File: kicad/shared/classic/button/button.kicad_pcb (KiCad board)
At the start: 2 copper layers, 22 x 45 mm, 6 parts, among them J2 Screw_Terminal_01x03, Q1 BC547

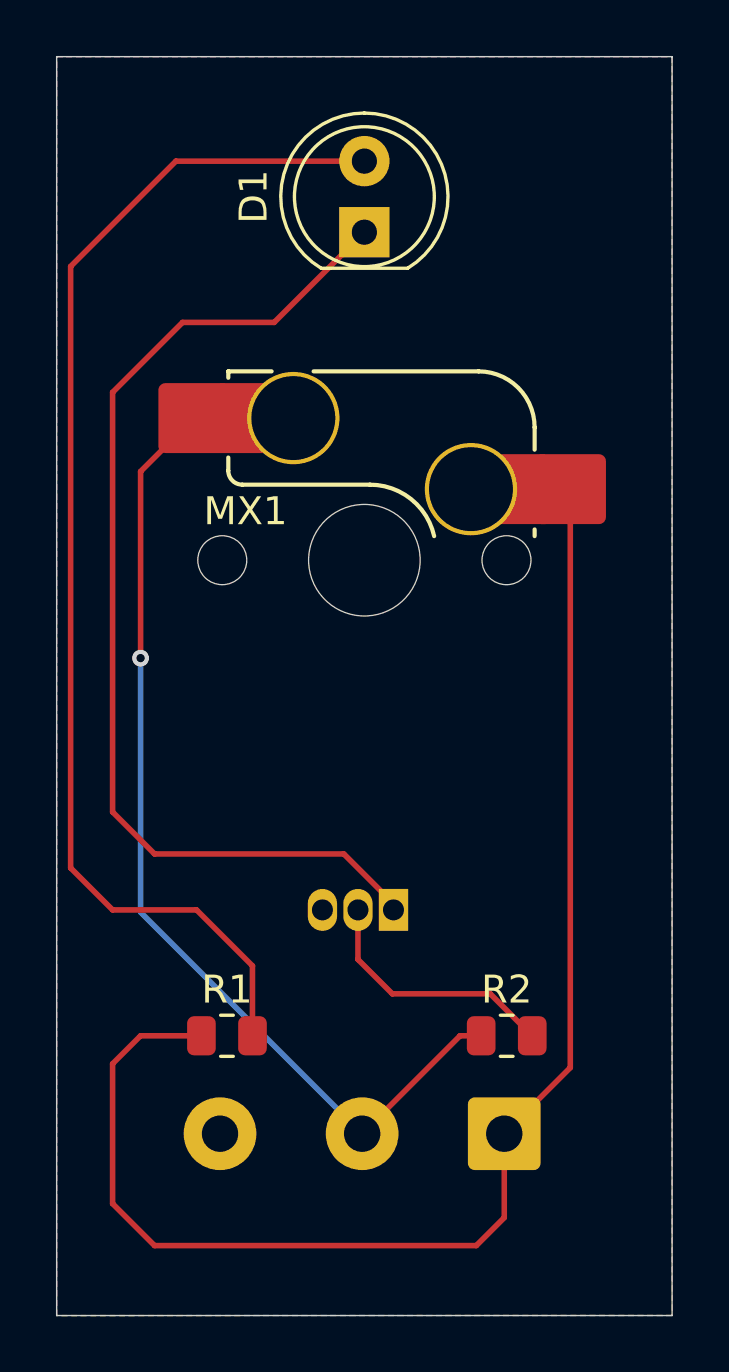
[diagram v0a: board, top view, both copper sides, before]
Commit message: Decoupling cap and JST-XA connector for Classic button daughterboard
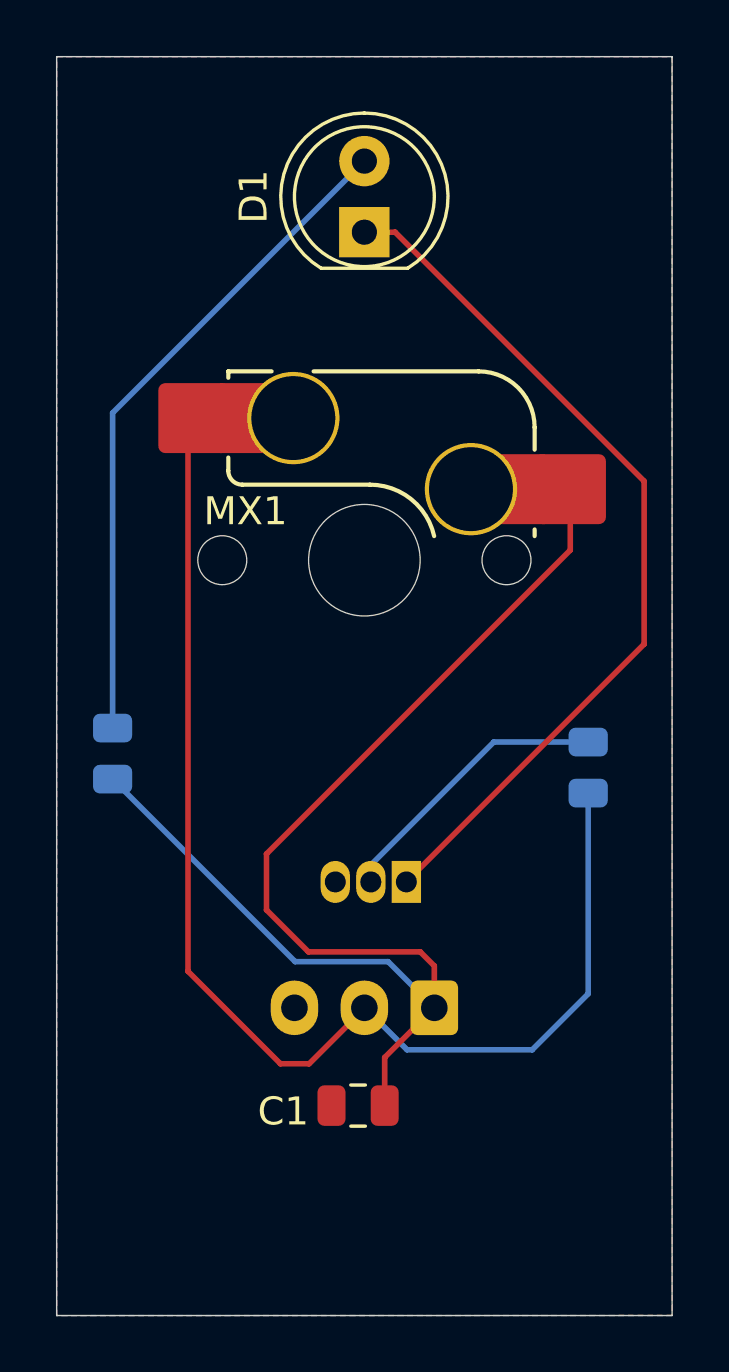
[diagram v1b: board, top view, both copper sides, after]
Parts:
- removed J2: Screw_Terminal_01x03, TerminalBlock_Phoenix:TerminalBlock_Phoenix_MKDS-1,5-3-5.08_1x03_P5.08mm_Horizontal
- added C1: 100n, Capacitor_SMD:C_0805_2012Metric, F.Cu at (139.3, 148.5)
- added J1: Conn_01x03, Connector_JST:JST_XA_S03B-XASK-1_1x03_P2.50mm_Horizontal, B.Cu at (142.0, 145.0)
- R1, R2: moved to B.Cu
- moved R1 10.9 mm to (130.5, 135.9), turned to 90 degrees
- moved R2 10.0 mm to (147.5, 136.4), turned to 90 degrees
- moved Q1 1.10 mm to (141.0, 140.5)
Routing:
- net Net-(D1-A): track 44.0 -> 24.0 mm
- net /SW_OUT: track 35.4 -> 45.0 mm, vias 1 -> 0
- net Net-(D1-K): track 38.0 -> 31.5 mm
- net +3V3: track 50.6 -> 47.0 mm
- net Net-(Q1-B): track 9.13 -> 10.2 mm

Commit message: Pulldown for the switch bc I'm dumb
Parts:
- added R3: 47k, Resistor_SMD:R_0805_2012Metric, B.Cu at (131.5, 151.5)
- C1: moved to B.Cu
- moved C1 8.29 mm to (147.6, 149.0)
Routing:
- net /SW_OUT: track 45.0 -> 55.3 mm
- net +3V3: track 47.0 -> 51.8 mm, vias 0 -> 1

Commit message: Button/LED assembly Classic actually does the thing properly now
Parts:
- removed J1: Conn_01x03, Connector_JST:JST_XA_S03B-XASK-1_1x03_P2.50mm_Horizontal
- added J2: Conn_01x04, Connector_JST:JST_XA_B04B-XASK-1-A_1x04_P2.50mm_Vertical, B.Cu at (143.5, 146.5)
- added R4: R, Resistor_SMD:R_0805_2012Metric, F.Cu at (134.5, 140.5)
- moved R3 11.1 mm to (131.5, 140.4)
- moved C1 3.58 mm to (148.0, 145.4), turned to 90 degrees
- moved R2 1.91 mm to (147.5, 134.5)
- moved R1 1.41 mm to (131.5, 134.9)
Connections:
- R2 pad 1: /SW_OUT -> /LED_IN
- R3 pad 1: /SW_OUT -> /LED_IN
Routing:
- net /SW_OUT: track 55.3 -> 26.9 mm
- net /LED_IN: track 0.00 -> 26.0 mm
- net +3V3: track 51.8 -> 38.9 mm
- net Net-(D1-K): track 31.5 -> 25.8 mm, vias 0 -> 1
- net Net-(D1-A): track 24.0 -> 22.6 mm
- net Net-(Q1-B): track 10.2 -> 11.5 mm
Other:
- board size 22 x 45 mm -> 20 x 40 mm

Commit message: feat: Cleaned up pin arrangement for Classic button/LED assembly, added connector for that on Classic control unit main board, added pins for STM32 TODO
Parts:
- R4: value R -> 47k
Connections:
- C1 pad 1: +3V3 -> GND
- C1 pad 2: GND -> +3V3
- J2 pad 1: +3V3 -> GND
- J2 pad 4: GND -> +3V3
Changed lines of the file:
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@@
 			)
 		)
-		(property "Value" "R"
+		(property "Value" "47k"
 			(at 0 1.65 90)
 			(layer "F.Fab")
@@
 			(remove_unused_layers no)
 			(roundrect_rratio 0.147059)
-			(net "+3V3")
+			(net "GND")
 			(pinfunction "Pin_1_1")
 			(pintype "passive")
@@
 			(layers "*.Cu" "*.Mask")
 			(remove_unused_layers no)
-			(net "GND")
+			(net "+3V3")
 			(pinfunction "Pin_4_4")
 			(pintype "passive")
@@
 			(layers "B.Cu" "B.Mask" "B.Paste")
 			(roundrect_rratio 0.25)
-			(net "+3V3")
+			(net "GND")
 			(pintype "passive")
 		)
@@
 			(layers "B.Cu" "B.Mask" "B.Paste")
 			(roundrect_rratio 0.25)
-			(net "GND")
-			(pintype "passive")
-		)
+			(net "+3V3")
+			(pintype "passive")
+		)

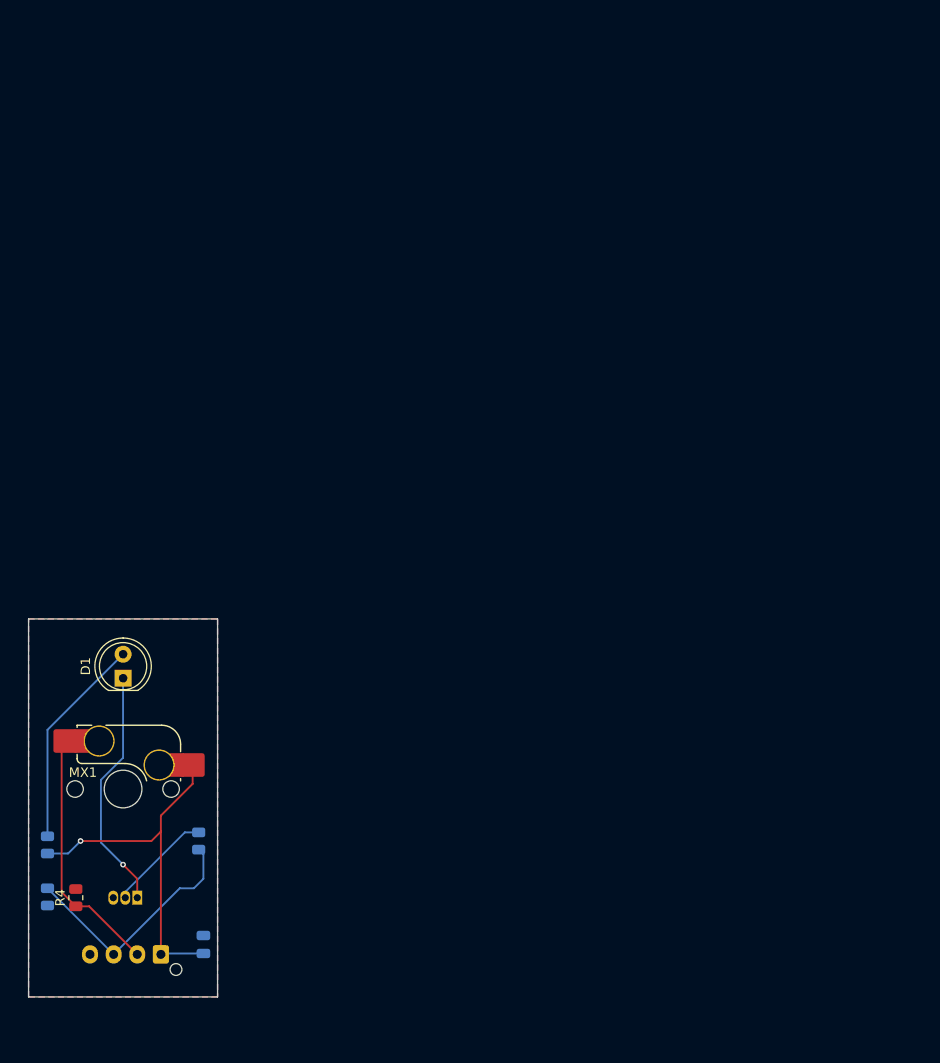
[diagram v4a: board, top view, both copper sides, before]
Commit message: feat: Routed prototype THT component boards for buzzer and button/LED assembly PCBs
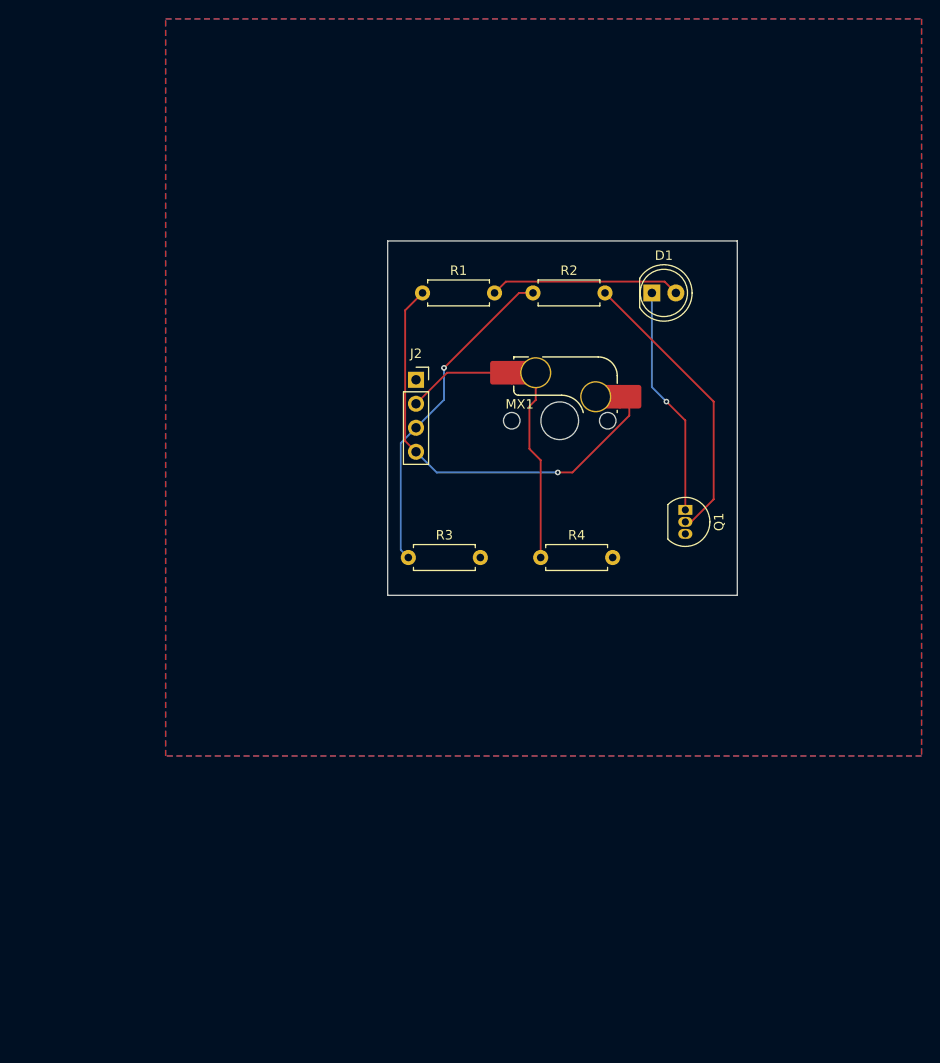
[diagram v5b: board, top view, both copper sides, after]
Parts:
- removed C1: 100n, Capacitor_SMD:C_0805_2012Metric
- J2: footprint Connector_JST:JST_XA_B04B-XASK-1-A_1x04_P2.50mm_Vertical -> Connector_PinSocket_2.54mm:PinSocket_1x04_P2.54mm_Vertical; moved to F.Cu
- Q1: moved to F.Cu
- R1, R2, R3: footprint Resistor_SMD:R_0805_2012Metric -> Resistor_THT:R_Axial_DIN0207_L6.3mm_D2.5mm_P7.62mm_Horizontal; moved to F.Cu
- R4: footprint Resistor_SMD:R_0805_2012Metric -> Resistor_THT:R_Axial_DIN0207_L6.3mm_D2.5mm_P7.62mm_Horizontal
- moved Q1 71.1 mm to (199.0, 99.5), turned to -90 degrees
- moved R1 70.6 mm to (171.2, 76.5), turned to 0 degrees
- moved D1 69.2 mm to (195.5, 76.5), turned to 0 degrees
- moved R2 67.9 mm to (182.9, 76.5), turned to 0 degrees
- moved J2 66.5 mm to (170.5, 85.7), turned to 0 degrees
- moved R4 61.0 mm to (183.7, 104.5), turned to 0 degrees
- moved MX1 60.5 mm to (185.7, 90.0)
- moved R3 52.4 mm to (169.7, 104.5), turned to 0 degrees
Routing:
- net Net-(Q1-B): track 11.5 -> 30.6 mm
- net /LED_IN: track 26.0 -> 35.0 mm, vias 0 -> 1
- net +3V3: track 38.9 -> 46.0 mm
- net /SW_OUT: track 26.9 -> 30.8 mm
- net Net-(D1-A): track 22.6 -> 20.2 mm
- net Net-(D1-K): track 25.8 -> 24.4 mm
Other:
- board size 20 x 40 mm -> 37 x 37.5 mm
